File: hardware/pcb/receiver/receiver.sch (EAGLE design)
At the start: 73 parts, among them IC1 REG1117, X2 B35N57

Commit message: hw: changed receiver ferrite bead filters inductance to 600ohm
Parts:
- added C34: 100u, rcl:CPOL-EU153CLV-0605
- JP1: MFR 54202-S08-04 -> 20021121-00008C4LF
- L4, L5, L6, L7: MFR 2508056007Y3 -> 2508056017Y2
- TR1: value MS40A -> ETC1-1T-2TR; device inductor-neosid:MS40A -> lstolcman_thesis:ETC1-1T-2TR; MFR (none) -> ETC1-1T-2TR
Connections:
- net GND: now also C34.-
- net N$1: now also TR1.3; no longer TR1.2
- net N$14: now also TR1.1; no longer TR1.4
- net N$15: now also TR1.2; no longer TR1.3
- net N$3: now also TR1.4; no longer TR1.1
- net N$7: now also C34.+
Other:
- note added: "jumper M50-2000005"
- note removed: "4:1 balun"
- moved on the sheet: D2, F1, J2
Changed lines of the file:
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@@
 <?xml version="1.0" encoding="utf-8"?>
 <!DOCTYPE eagle SYSTEM "eagle.dtd">
-<eagle version="7.4.0">
+<eagle version="7.5.0">
 <drawing>
 <settings>
@@
 <attribute name="MFR" value="CDSOD323-T03C"/>
 </part>
-<part name="TR1" library="inductor-neosid" deviceset="MS40" device="A"/>
 <part name="GND7" library="supply1" deviceset="GND" device=""/>
 <part name="GND8" library="supply1" deviceset="GND" device=""/>
@@
 </part>
 <part name="JP1" library="lstolcman_thesis" deviceset="PINHD-2X4" device="">
-<attribute name="MFR" value="54202-S08-04"/>
+<attribute name="MFR" value="20021121-00008C4LF"/>
 </part>
 <part name="GND19" library="supply1" deviceset="GND" device=""/>
 <part name="L7" library="inductor-neosid" deviceset="SM-NE29" device="" value="ferrite bead">
-<attribute name="MFR" value="2508056007Y3"/>
+<attribute name="MFR" value="2508056017Y2"/>
 </part>
 <part name="C33" library="rcl" deviceset="C-EU" device="C0805" value="100p">
@@
 <part name="GND5" library="supply1" deviceset="GND" device=""/>
 <part name="L4" library="inductor-neosid" deviceset="SM-NE29" device="" value="ferrite bead">
-<attribute name="MFR" value="2508056007Y3"/>
+<attribute name="MFR" value="2508056017Y2"/>
 </part>
 <part name="L6" library="inductor-neosid" deviceset="SM-NE29" device="" value="ferrite bead">
-<attribute name="MFR" value="2508056007Y3"/>
+<attribute name="MFR" value="2508056017Y2"/>
 </part>
 <part name="L5" library="inductor-neosid" deviceset="SM-NE29" device="" value="ferrite bead">
-<attribute name="MFR" value="2508056007Y3"/>
+<attribute name="MFR" value="2508056017Y2"/>
 </part>
 <part name="X2" library="con-coax" deviceset="B35N57" device=""/>
+<part name="C34" library="rcl" deviceset="CPOL-EU" device="153CLV-0605" value="100u">
+<attribute name="MFR" value="VE-470M1ETR-0605"/>
+</part>
+<part name="TR1" library="lstolcman_thesis" deviceset="ETC1-1T-2TR" device="">
+<attribute name="MFR" value="ETC1-1T-2TR"/>
+</part>
 </parts>
 <sheets>
 <sheet>
 <plain>
-<text x="-185.42" y="68.58" size="1.778" layer="97">4:1 balun</text>
 <wire x1="-287.02" y1="78.74" x2="-287.02" y2="30.48" width="0.1524" layer="97" style="shortdash"/>
 <wire x1="-287.02" y1="30.48" x2="-203.2" y2="30.48" width="0.1524" layer="97" style="shortdash"/>
@@
 <wire x1="-203.2" y1="-15.24" x2="-203.2" y2="22.86" width="0.1524" layer="97" style="shortdash"/>
 <wire x1="-203.2" y1="22.86" x2="-264.16" y2="22.86" width="0.1524" layer="97" style="shortdash"/>
+<text x="91.44" y="50.8" size="1.778" layer="97">jumper
+M50-2000005</text>
 </plain>
 <instances>
@@
 <attribute name="MFR" x="-297.18" y="63.5" size="2.54" layer="96" rot="R90" display="off"/>
 </instance>
-<instance part="GND3" gate="1" x="-256.54" y="269.24"/>
-<instance part="J2" gate="G$1" x="-264.16" y="279.4">
-<attribute name="MFR" x="-264.16" y="279.4" size="1.778" layer="96" display="off"/>
+<instance part="GND3" gate="1" x="-269.24" y="269.24"/>
+<instance part="J2" gate="G$1" x="-276.86" y="279.4">
+<attribute name="MFR" x="-276.86" y="279.4" size="1.778" layer="96" display="off"/>
 </instance>
 <instance part="R1" gate="G$1" x="137.16" y="35.56">
@@
 <attribute name="MFR" x="-304.8" y="55.88" size="2.54" layer="96" rot="R90" display="off"/>
 </instance>
-<instance part="TR1" gate="G$1" x="-182.88" y="58.42"/>
 <instance part="GND7" gate="1" x="-190.5" y="35.56"/>
 <instance part="GND8" gate="1" x="-175.26" y="35.56"/>
@@
 <instance part="GND12" gate="1" x="-208.28" y="43.18"/>
 <instance part="P+5" gate="1" x="-172.72" y="292.1"/>
-<instance part="GND13" gate="1" x="-218.44" y="264.16"/>
+<instance part="GND13" gate="1" x="-223.52" y="264.16"/>
 <instance part="GND14" gate="1" x="-172.72" y="264.16"/>
 <instance part="GND15" gate="1" x="-198.12" y="264.16"/>
@@
 <attribute name="MFR" x="-213.36" y="274.32" size="2.54" layer="96" rot="MR180" display="off"/>
 </instance>
-<instance part="F1" gate="G$1" x="-233.68" y="281.94">
-<attribute name="MFR" x="-233.68" y="281.94" size="2.54" layer="96" display="off"/>
-</instance>
-<instance part="D2" gate="G$1" x="-248.92" y="281.94">
-<attribute name="MFR" x="-248.92" y="281.94" size="2.54" layer="96" display="off"/>
+<instance part="F1" gate="G$1" x="-246.38" y="281.94">
+<attribute name="MFR" x="-246.38" y="281.94" size="2.54" layer="96" display="off"/>
+</instance>
+<instance part="D2" gate="G$1" x="-261.62" y="281.94">
+<attribute name="MFR" x="-261.62" y="281.94" size="2.54" layer="96" display="off"/>
 </instance>
 <instance part="R5" gate="G$1" x="-167.64" y="63.5">
@@
 </instance>
 <instance part="X2" gate="G$1" x="-337.82" y="63.5"/>
+<instance part="C34" gate="G$1" x="-233.68" y="276.86">
+<attribute name="MFR" x="-233.68" y="276.86" size="1.778" layer="96" display="off"/>
+</instance>
+<instance part="TR1" gate="G$1" x="-182.88" y="58.42">
+<attribute name="MFR" x="-182.88" y="58.42" size="1.778" layer="96" display="off"/>
+</instance>
 </instances>
 <busses>
@@
 <pinref part="GND3" gate="1" pin="GND"/>
 <pinref part="J2" gate="G$1" pin="1"/>
-<wire x1="-256.54" y1="276.86" x2="-256.54" y2="271.78" width="0.1524" layer="91"/>
-<wire x1="-259.08" y1="276.86" x2="-256.54" y2="276.86" width="0.1524" layer="91"/>
+<wire x1="-269.24" y1="276.86" x2="-269.24" y2="271.78" width="0.1524" layer="91"/>
+<wire x1="-271.78" y1="276.86" x2="-269.24" y2="276.86" width="0.1524" layer="91"/>
 <pinref part="J2" gate="G$1" pin="2"/>
-<wire x1="-259.08" y1="279.4" x2="-256.54" y2="279.4" width="0.1524" layer="91"/>
-<wire x1="-256.54" y1="279.4" x2="-256.54" y2="276.86" width="0.1524" layer="91"/>
-<junction x="-256.54" y="276.86"/>
+<wire x1="-271.78" y1="279.4" x2="-269.24" y2="279.4" width="0.1524" layer="91"/>
+<wire x1="-269.24" y1="279.4" x2="-269.24" y2="276.86" width="0.1524" layer="91"/>
+<junction x="-269.24" y="276.86"/>
 </segment>
 <segment>
@@
 </segment>
 <segment>
-<pinref part="TR1" gate="G$1" pin="5"/>
 <wire x1="-187.96" y1="53.34" x2="-190.5" y2="53.34" width="0.1524" layer="91"/>
 <wire x1="-190.5" y1="53.34" x2="-190.5" y2="38.1" width="0.1524" layer="91"/>
 <pinref part="GND7" gate="1" pin="GND"/>
+<pinref part="TR1" gate="G$1" pin="5"/>
 </segment>
 <segment>
@@
 <segment>
 <wire x1="-223.52" y1="271.78" x2="-223.52" y2="269.24" width="0.1524" layer="91"/>
-<wire x1="-223.52" y1="269.24" x2="-218.44" y2="269.24" width="0.1524" layer="91"/>
-<wire x1="-218.44" y1="269.24" x2="-213.36" y2="269.24" width="0.1524" layer="91"/>
+<wire x1="-223.52" y1="269.24" x2="-213.36" y2="269.24" width="0.1524" layer="91"/>
 <wire x1="-213.36" y1="269.24" x2="-213.36" y2="271.78" width="0.1524" layer="91"/>
 <pinref part="GND13" gate="1" pin="GND"/>
-<wire x1="-218.44" y1="266.7" x2="-218.44" y2="269.24" width="0.1524" layer="91"/>
-<junction x="-218.44" y="269.24"/>
+<wire x1="-223.52" y1="266.7" x2="-223.52" y2="269.24" width="0.1524" layer="91"/>
+<junction x="-223.52" y="269.24"/>
 <pinref part="C40" gate="G$1" pin="2"/>
 <pinref part="C31" gate="G$1" pin="1"/>
+<pinref part="C34" gate="G$1" pin="-"/>
+<wire x1="-223.52" y1="269.24" x2="-233.68" y2="269.24" width="0.1524" layer="91"/>
+<wire x1="-233.68" y1="269.24" x2="-233.68" y2="271.78" width="0.1524" layer="91"/>
+<junction x="-223.52" y="269.24"/>
 </segment>
 <segment>
@@
 <net name="N$1" class="0">
 <segment>
-<pinref part="TR1" gate="G$1" pin="2"/>
 <wire x1="-172.72" y1="63.5" x2="-180.34" y2="63.5" width="0.1524" layer="91"/>
 <pinref part="R5" gate="G$1" pin="1"/>
+<pinref part="TR1" gate="G$1" pin="3"/>
 </segment>
 </net>
 <net name="N$14" class="0">
 <segment>
-<pinref part="TR1" gate="G$1" pin="4"/>
 <wire x1="-172.72" y1="53.34" x2="-180.34" y2="53.34" width="0.1524" layer="91"/>
 <pinref part="R6" gate="G$1" pin="1"/>
+<pinref part="TR1" gate="G$1" pin="1"/>
 </segment>
 </net>
 <net name="N$15" class="0">
 <segment>
-<pinref part="TR1" gate="G$1" pin="3"/>
 <wire x1="-180.34" y1="58.42" x2="-175.26" y2="58.42" width="0.1524" layer="91"/>
 <wire x1="-175.26" y1="58.42" x2="-175.26" y2="48.26" width="0.1524" layer="91"/>
 <pinref part="C37" gate="G$1" pin="2"/>
+<pinref part="TR1" gate="G$1" pin="2"/>
 </segment>
 </net>
@@
 <net name="N$3" class="0">
 <segment>
-<pinref part="TR1" gate="G$1" pin="1"/>
 <wire x1="-190.5" y1="63.5" x2="-187.96" y2="63.5" width="0.1524" layer="91"/>
 <pinref part="C36" gate="G$1" pin="2"/>
+<pinref part="TR1" gate="G$1" pin="4"/>
 </segment>
 </net>
@@
 <pinref part="C31" gate="G$1" pin="2"/>
 <pinref part="F1" gate="G$1" pin="2"/>
-<wire x1="-223.52" y1="281.94" x2="-228.6" y2="281.94" width="0.1524" layer="91"/>
+<wire x1="-223.52" y1="281.94" x2="-233.68" y2="281.94" width="0.1524" layer="91"/>
 <junction x="-223.52" y="281.94"/>
+<pinref part="C34" gate="G$1" pin="+"/>
+<wire x1="-233.68" y1="281.94" x2="-241.3" y2="281.94" width="0.1524" layer="91"/>
+<wire x1="-233.68" y1="279.4" x2="-233.68" y2="281.94" width="0.1524" layer="91"/>
+<junction x="-233.68" y="281.94"/>
 </segment>
 </net>
@@
 <segment>
 <pinref part="F1" gate="G$1" pin="1"/>
-<wire x1="-246.38" y1="281.94" x2="-241.3" y2="281.94" width="0.1524" layer="91"/>
+<wire x1="-259.08" y1="281.94" x2="-254" y2="281.94" width="0.1524" layer="91"/>
 <pinref part="D2" gate="G$1" pin="C"/>
 </segment>
@@
 <pinref part="D2" gate="G$1" pin="A"/>
 <pinref part="J2" gate="G$1" pin="3"/>
-<wire x1="-251.46" y1="281.94" x2="-259.08" y2="281.94" width="0.1524" layer="91"/>
-</segment>
-</net>
+<wire x1="-264.16" y1="281.94" x2="-271.78" y2="281.94" width="0.1524" layer="91"/>
+</segment>
+</net>

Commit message: hw: minor changes
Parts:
- removed C32: 100n, rcl:C-EUC0805
- added C35, C38, C41, C43: 4,7u, rcl:C-EUC0805
- added C42: 100n, rcl:C-EUC0805
- C10, C14, C9: value 100p -> (none); MFR C0805C101J5GACTU -> (none)
- C11: value 68p -> (none); MFR C0805C680J5GACTU -> (none)
- C12: value 82p -> (none); MFR 08055A820JAT2A -> (none)
- C13: value 18p -> (none); MFR C0805C180J5GACTU -> (none)
- C15: value 62p -> (none); MFR 08051A620JAT2A -> (none)
- C21: MFR 08056D475KAT2A -> JMK212BJ475KG-T
- IC1: value REG1117 -> (none); device burr-brown:REG1117 -> lstolcman_thesis:REG1117; MFR NCV1117ST50T3G -> NCP1117DT50G; SUP (none) -> tme
- J2: MFR 163-179PH-EX -> FC68148; SUP (none) -> tme
- L1: value 120n -> (none); MFR CE201210-R12J -> (none)
- L2: value 68n -> (none); MFR CE201210-68NJ -> (none)
- L3: value 82n -> (none); MFR CE201210-82NJ -> (none)
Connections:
- net +3V3: now also C42.2; no longer C23.2, C24.2, C25.2, C26.2, C27.2, C28.2, C29.2
- net +3V3A_ADC: now also C23.2, C24.2, C25.2, C26.2, C27.2, C28.2, C29.2, C43.1; no longer C32.1
- net +5V_AMP: now also C41.1
- net GND: now also C35.2, C38.2, C41.2, C42.1, C43.2; no longer C32.2
- net VDD: now also C35.1, C38.1
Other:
- note added: "adc analog vcc fitlering"
- note added: "adc digital vcc fitlering"
- note removed: "adc digital and analog vcc fitlering"
- moved on the sheet: C17, C2, C23, C24, C25, C26, C27, C28, C29, C3, C4, C5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

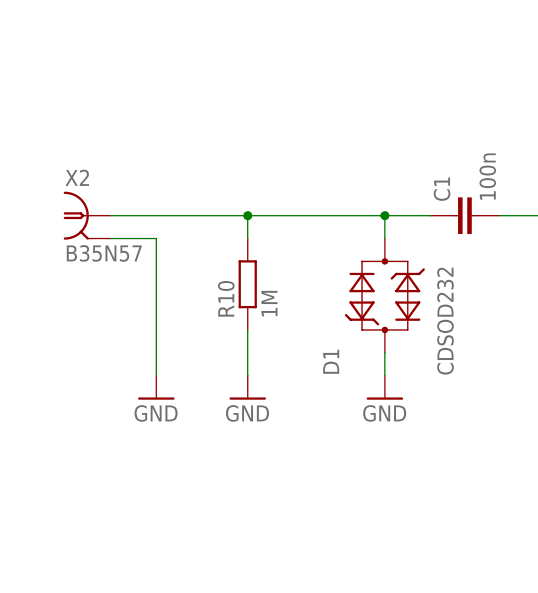
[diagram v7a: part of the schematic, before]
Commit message: hw: bnc connector, misc changes
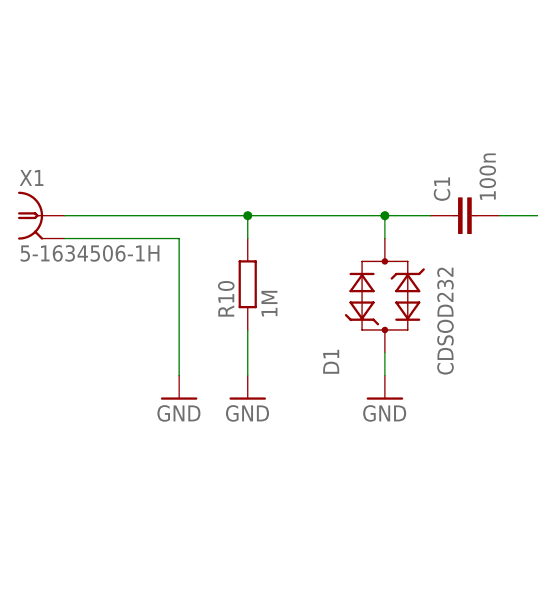
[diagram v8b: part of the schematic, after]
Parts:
- removed X2: B35N57, con-coax:B35N57
- added X1: 5-1634506-1H, lstolcman_thesis:5-1634506-1H
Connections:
- net GND: now also X1.2; no longer X2.2
- net N$2: now also X1.1; no longer X2.1
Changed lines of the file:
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@@
 <attribute name="MFR" value="2508056017Y2"/>
 </part>
-<part name="X2" library="con-coax" deviceset="B35N57" device=""/>
 <part name="C34" library="rcl" deviceset="CPOL-EU" device="153CLV-0605" value="100u">
 <attribute name="MFR" value="VE-470M1ETR-0605"/>
@@
 <part name="+3V1" library="supply1" deviceset="+3V3" device=""/>
 <part name="+3V8" library="supply1" deviceset="+3V3" device=""/>
+<part name="X1" library="lstolcman_thesis" deviceset="5-1634506-1" device="" technology="H">
+<attribute name="MFR" value="5-1634506-1"/>
+</part>
 </parts>
 <sheets>
@@
 <instances>
 <instance part="GND1" gate="1" x="-304.8" y="43.18"/>
-<instance part="GND2" gate="1" x="-330.2" y="43.18"/>
+<instance part="GND2" gate="1" x="-327.66" y="43.18"/>
 <instance part="C1" gate="G$1" x="-297.18" y="63.5" rot="R90">
 <attribute name="MFR" x="-297.18" y="63.5" size="2.54" layer="96" rot="R90" display="off"/>
@@
 <attribute name="MFR" x="-254" y="5.08" size="1.778" layer="96" rot="MR0" display="off"/>
 </instance>
-<instance part="X2" gate="G$1" x="-337.82" y="63.5"/>
 <instance part="C34" gate="G$1" x="-233.68" y="276.86">
 <attribute name="MFR" x="-233.68" y="276.86" size="1.778" layer="96" display="off"/>
@@
 <instance part="+3V1" gate="G$1" x="-43.18" y="233.68"/>
 <instance part="+3V8" gate="G$1" x="-129.54" y="233.68"/>
+<instance part="X1" gate="G$1" x="-342.9" y="63.5">
+<attribute name="MFR" x="-342.9" y="63.5" size="1.778" layer="96" display="off"/>
+</instance>
 </instances>
 <busses>
@@
 <net name="GND" class="0">
 <segment>
-<wire x1="-335.28" y1="60.96" x2="-330.2" y2="60.96" width="0.1524" layer="91"/>
-<wire x1="-330.2" y1="60.96" x2="-330.2" y2="45.72" width="0.1524" layer="91"/>
+<wire x1="-340.36" y1="60.96" x2="-327.66" y2="60.96" width="0.1524" layer="91"/>
+<wire x1="-327.66" y1="60.96" x2="-327.66" y2="45.72" width="0.1524" layer="91"/>
 <pinref part="GND2" gate="1" pin="GND"/>
-<pinref part="X2" gate="G$1" pin="2"/>
+<pinref part="X1" gate="G$1" pin="2"/>
 </segment>
 <segment>
@@
 <pinref part="R10" gate="G$1" pin="2"/>
 <wire x1="-320.04" y1="63.5" x2="-320.04" y2="60.96" width="0.1524" layer="91"/>
-<wire x1="-320.04" y1="63.5" x2="-335.28" y2="63.5" width="0.1524" layer="91"/>
+<wire x1="-320.04" y1="63.5" x2="-340.36" y2="63.5" width="0.1524" layer="91"/>
 <junction x="-320.04" y="63.5"/>
 <wire x1="-304.8" y1="63.5" x2="-320.04" y2="63.5" width="0.1524" layer="91"/>
 <junction x="-304.8" y="63.5"/>
-<pinref part="X2" gate="G$1" pin="1"/>
+<pinref part="X1" gate="G$1" pin="1"/>
 </segment>
 </net>
